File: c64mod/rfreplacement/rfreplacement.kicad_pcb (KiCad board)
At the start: 2 copper layers, 63.5 x 64.8 mm, 94 parts, among them SW1 SW_SP3T, U2 10M02SCE144, Y1 Conn_Coaxial

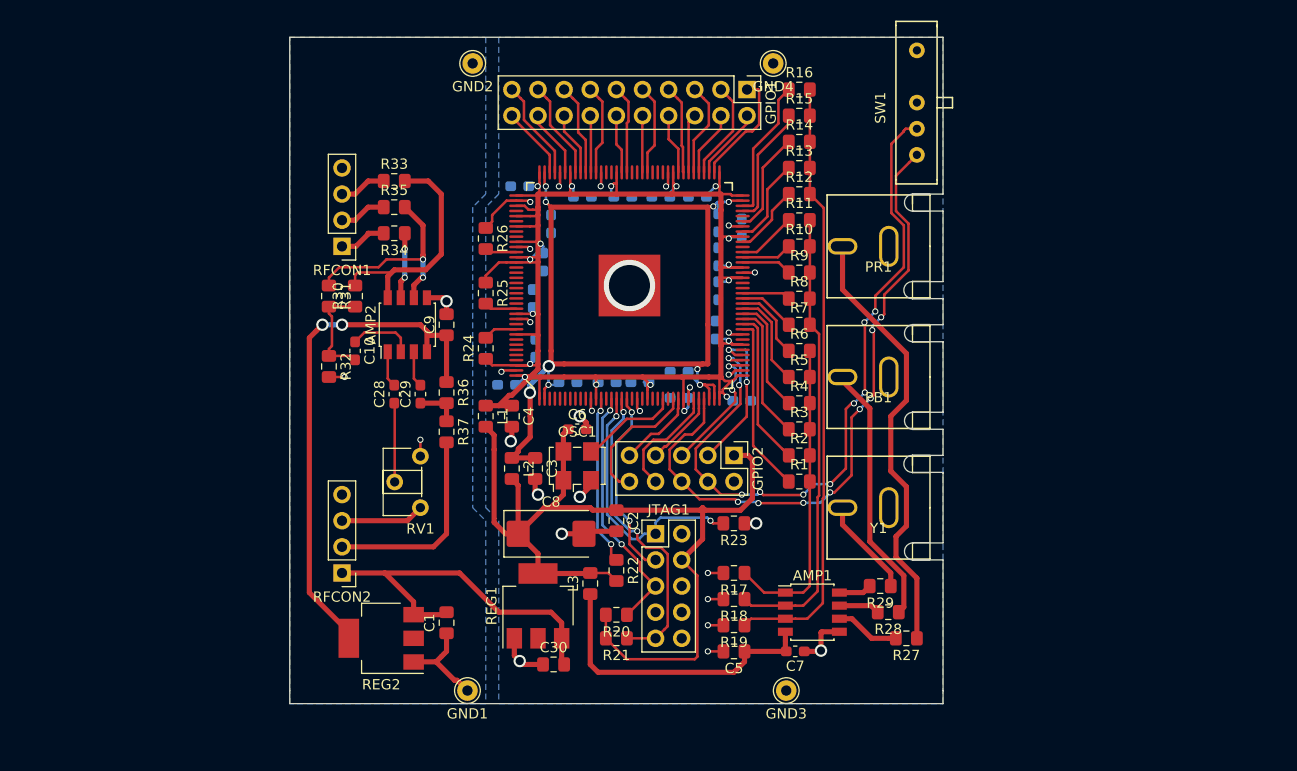
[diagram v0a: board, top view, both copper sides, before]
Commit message: C64 mod: fit rf replacement to long and short main boards
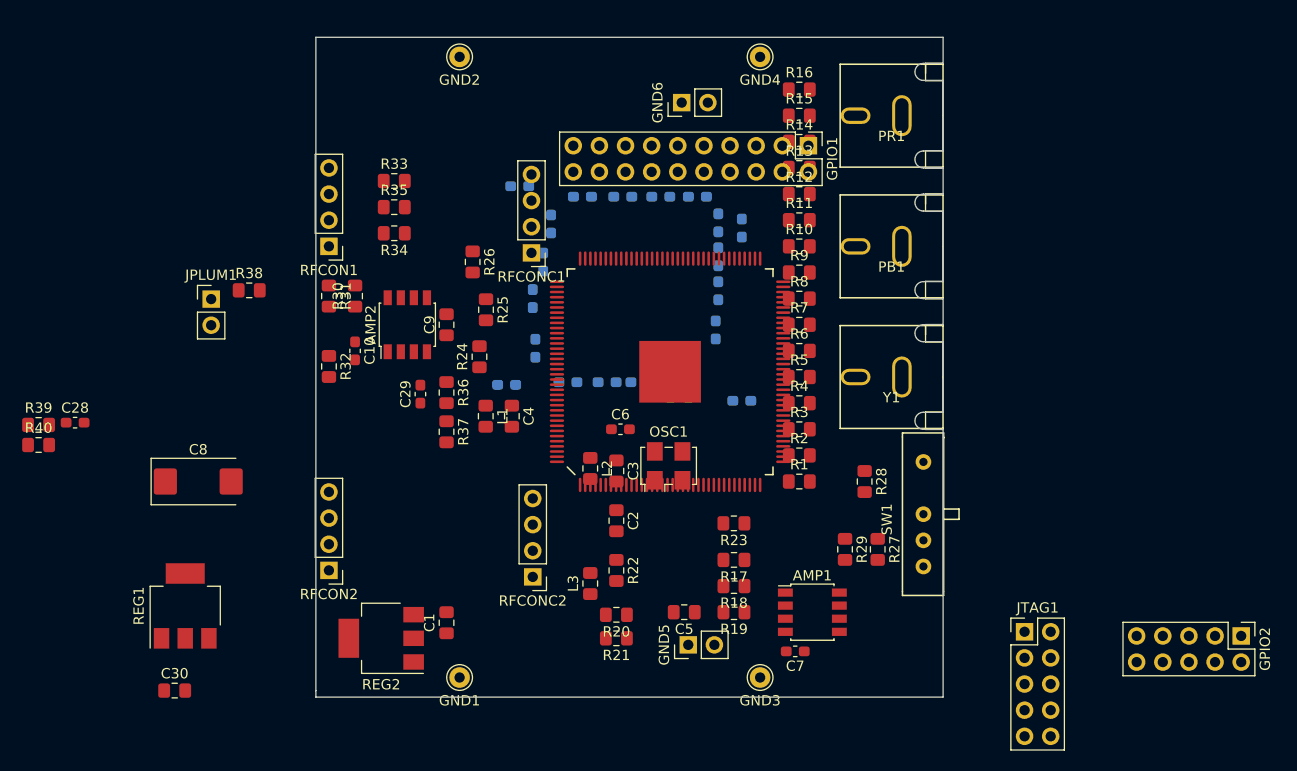
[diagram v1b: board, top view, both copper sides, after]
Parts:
- removed RV1: 1k, Potentiometer_THT:Potentiometer_ACP_CA6-H2,5_Horizontal
- added GND5: Conn_01x02, Connector_PinHeader_2.54mm:PinHeader_1x02_P2.54mm_Vertical, F.Cu at (140.3, 109.9)
- added GND6: Conn_01x02, Connector_PinHeader_2.54mm:PinHeader_1x02_P2.54mm_Vertical, F.Cu at (139.7, 57.1)
- added JPLUM1: Jumper_2_Open, Connector_PinHeader_2.54mm:PinHeader_1x02_P2.54mm_Vertical, F.Cu at (94.0, 76.2)
- added R38: 680, Resistor_SMD:R_0805_2012Metric_Pad1.15x1.40mm_HandSolder, F.Cu at (97.7, 75.4)
- added R39: 680, Resistor_SMD:R_0805_2012Metric_Pad1.15x1.40mm_HandSolder, F.Cu at (77.2, 88.5)
- added R40: 330, Resistor_SMD:R_0805_2012Metric_Pad1.15x1.40mm_HandSolder, F.Cu at (77.2, 90.4)
- added RFCONC1: Conn_01x04, Connector_PinHeader_2.54mm:PinHeader_1x04_P2.54mm_Vertical, F.Cu at (125.1, 71.8)
- added RFCONC2: Conn_01x04, Connector_PinHeader_2.54mm:PinHeader_1x04_P2.54mm_Vertical, F.Cu at (125.2, 103.3)
- R36: value 150 -> 680
- R37: value 310 -> 330
- moved GPIO2 52.3 mm to (194.1, 109.0)
- moved SW1 40.0 mm to (160.7, 97.2)
- moved JTAG1 37.1 mm to (173.0, 108.6)
- moved C30 36.9 mm to (90.4, 114.3)
- moved C8 34.7 mm to (92.7, 94.0)
- moved REG1 34.3 mm to (91.4, 106.1)
- moved C28 31.1 mm to (80.7, 88.3), turned to 0 degrees
- moved R28 12.9 mm to (157.5, 94.0), turned to 270 degrees
- moved PR1 12.8 mm to (165.1, 58.4)
- moved Y1 12.8 mm to (165.1, 83.8)
- moved PB1 12.8 mm to (165.1, 71.1)
- moved U2 9.27 mm to (138.6, 83.3)
- moved R27 9.08 mm to (158.8, 100.6), turned to 270 degrees
- moved OSC1 8.89 mm to (138.4, 92.5)
- moved GPIO1 8.09 mm to (152.0, 61.3)
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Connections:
- R36 pad 2: Net-(C29-Pad1) -> Net-(JPLUM1-Pad1)
- R37 pad 1: Net-(C29-Pad1) -> /3V3X
- R37 pad 2: /LUMA_IN -> Net-(C29-Pad1)
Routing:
- net /3V3B: track 178.1 -> 0.00 mm, vias 18 -> 0
- net /3V3A: track 98.0 -> 0.00 mm
- net /3V3C: track 97.2 -> 0.00 mm, vias 9 -> 0
- net Net-(GPIO2-Pad4): track 69.5 -> 0.00 mm, vias 10 -> 0
- net Net-(GPIO2-Pad6): track 63.8 -> 0.00 mm, vias 8 -> 0
- net Net-(AMP1-Pad3): track 59.0 -> 0.00 mm
- net GND: track 53.0 -> 0.00 mm, vias 27 -> 0
- net /3V3X: track 51.0 -> 0.00 mm, vias 2 -> 0
- net Net-(AMP1-Pad2): track 44.4 -> 0.00 mm
- net /PR: track 43.2 -> 0.00 mm
- net +12V: track 36.0 -> 0.00 mm
- net Net-(JTAG1-Pad9): track 30.6 -> 0.00 mm, vias 2 -> 0
- net Net-(AMP1-Pad1): track 30.3 -> 0.00 mm
- net /3V3D: track 29.6 -> 0.00 mm
- net Net-(JTAG1-Pad1): track 25.7 -> 0.00 mm, vias 2 -> 0
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- removed copper zone on B.Cu, net GND
- removed copper zone on B.Cu, net GNDA
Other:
- board size 63.5 x 64.8 mm -> 61 x 64.1 mm

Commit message: Layout RF replacement board
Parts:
- removed GND6: Conn_01x02, Connector_PinHeader_2.54mm:PinHeader_1x02_P2.54mm_Vertical
- removed GPIO2: Conn_02x05_Odd_Even, Connector_PinHeader_2.54mm:PinHeader_2x05_P2.54mm_Vertical
- removed PB1, PR1, Y1: Conn_Coaxial, footprints:RCA_JACK
- added J1: AudioJack4_Ground, footprints:Conrad 4pin audio jack, F.Cu at (167.0, 69.8)
- C6, C7, C9: moved to B.Cu
- C8: footprint Capacitor_Tantalum_SMD:CP_EIA-7343-15_Kemet-W_Pad2.25x2.55mm_HandSolder -> Capacitor_SMD:CP_Elec_6.3x5.8
- moved REG1 39.5 mm to (130.8, 109.2), turned to 0 degrees
- moved C8 38.6 mm to (130.8, 100.3), turned to 90 degrees
- moved C28 35.7 mm to (113.0, 73.0), turned to 90 degrees
- moved JTAG1 35.5 mm to (137.5, 109.2), turned to 90 degrees
- moved R19 35.5 mm to (162.1, 75.7), turned to 0 degrees
- moved R40 35.0 mm to (110.5, 79.8), turned to 90 degrees
- moved C30 34.4 mm to (124.5, 109.5), turned to 270 degrees
- moved GND5 33.8 mm to (162.6, 84.5), turned to 180 degrees
- moved R39 33.6 mm to (110.5, 83.8), turned to 90 degrees
- moved L1 31.5 mm to (149.1, 101.1)
- moved R18 31.3 mm to (162.1, 78.0), turned to 0 degrees
- moved JPLUM1 27.4 mm to (118.5, 88.5)
- moved C4 25.9 mm to (147.3, 97.0), turned to 180 degrees
- moved C34 24.9 mm to (143.9, 93.7), turned to 180 degrees
- moved C2 23.7 mm to (152.9, 111.1), turned to 0 degrees
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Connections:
- AMP1 pad 6: /PR1 -> /PY1
- AMP1 pad 8: /PY1 -> /PR1
- R1 pad 2: Net-(AMP1-Pad1) -> Net-(AMP1-Pad3)
- R12 pad 2: Net-(AMP1-Pad3) -> Net-(AMP1-Pad1)
- R13 pad 2: Net-(AMP1-Pad3) -> Net-(AMP1-Pad1)
- R14 pad 2: Net-(AMP1-Pad3) -> Net-(AMP1-Pad1)
- R15 pad 2: Net-(AMP1-Pad3) -> Net-(AMP1-Pad1)
- R16 pad 2: Net-(AMP1-Pad3) -> Net-(AMP1-Pad1)
- R17 pad 1: Net-(AMP1-Pad1) -> Net-(AMP1-Pad3)
- R19 pad 1: Net-(AMP1-Pad3) -> Net-(AMP1-Pad1)
- R2 pad 2: Net-(AMP1-Pad1) -> Net-(AMP1-Pad3)
- R3 pad 2: Net-(AMP1-Pad1) -> Net-(AMP1-Pad3)
- R4 pad 2: Net-(AMP1-Pad1) -> Net-(AMP1-Pad3)
- R5 pad 2: Net-(AMP1-Pad1) -> Net-(AMP1-Pad3)
- R6 pad 2: Net-(AMP1-Pad1) -> Net-(AMP1-Pad3)
- SW1 pad 1: Net-(GPIO2-Pad6) -> Net-(SW1-Pad1)
- U2 pad 33: Net-(GPIO2-Pad6) -> Net-(U2-Pad33)
- U2 pad 39: Net-(GPIO2-Pad5) -> Net-(SW1-Pad1)
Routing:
- net /3V3B: track 0.00 -> 178.8 mm, vias 0 -> 17
- net /3V3C: track 0.00 -> 92.2 mm, vias 0 -> 9
- net /3V3A: track 0.00 -> 74.1 mm, vias 0 -> 2
- net /3V3X: track 0.00 -> 59.7 mm, vias 0 -> 3
- net /PB: track 0.00 -> 49.7 mm, vias 0 -> 1
- net GND: track 0.00 -> 48.6 mm, vias 0 -> 25
- net /PR: track 0.00 -> 48.1 mm, vias 0 -> 1
- net Net-(AMP1-Pad1): track 0.00 -> 45.9 mm
- net /Y: track 0.00 -> 44.0 mm, vias 0 -> 1
- net /COMPOSITE_OUT: track 0.00 -> 43.9 mm, vias 0 -> 3
- net +12V: track 0.00 -> 39.9 mm
- net Net-(AMP1-Pad2): track 0.00 -> 36.0 mm
- net /CHROMA_IN: track 0.00 -> 34.6 mm, vias 0 -> 2
- net /LUMA_OUT: track 0.00 -> 34.3 mm, vias 0 -> 2
- net /CHROMA_OUT: track 0.00 -> 34.2 mm
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- added copper zone on B.Cu, net GND
- added copper zone on B.Cu, net GNDA
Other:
- outline, holes or cut-outs redrawn

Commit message: Finished RF replacement  board for C64
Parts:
- C9: moved to F.Cu
- JPLUM1: footprint Connector_PinHeader_2.54mm:PinHeader_1x02_P2.54mm_Vertical -> Jumper:SolderJumper-2_P1.3mm_Open_RoundedPad1.0x1.5mm
- moved C9 12.4 mm to (120.1, 78.2), turned to 270 degrees
- moved JPLUM1 3.68 mm to (118.5, 92.2), turned to 270 degrees
- moved C20 2.47 mm to (130.3, 93.5), turned to 0 degrees
- moved C21 2.05 mm to (129.7, 71.5), turned to 0 degrees
- moved RFCONC1 0.64 mm to (125.7, 71.1)
- moved RFCONC2 0.64 mm to (125.7, 102.6)
- moved SW1 0.64 mm to (160.7, 96.5)
- moved R19 0.51 mm to (162.1, 75.2)
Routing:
- net Net-(SW1-Pad2): track 21.9 -> 32.7 mm
- net +12V: track 39.9 -> 44.4 mm
- net /3V3B: track 178.8 -> 182.0 mm
- net Net-(JPLUM1-Pad1): track 3.09 -> 6.12 mm
- net GNDA: track 11.1 -> 12.6 mm, vias 4 -> 5
- net /3V3C: track 92.2 -> 93.5 mm
- net Net-(AMP2-Pad8): track 16.8 -> 15.5 mm
- net Net-(AMP1-Pad2): track 36.0 -> 35.0 mm
- net Net-(AMP1-Pad1): track 45.9 -> 45.1 mm, vias 0 -> 2
- net Net-(SW1-Pad1): track 24.3 -> 25.1 mm
- net /LUMA_OUT: track 34.3 -> 34.9 mm
- net /COMPOSITE_OUT: track 43.9 -> 44.5 mm
- net /CHROMA_OUT: track 34.2 -> 34.9 mm
- net /CHROMA_IN: track 34.6 -> 35.2 mm
- net /LUMA_IN: track 33.7 -> 34.3 mm
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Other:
- board text added: "C64 Video Enhancement github.com/c0pperdragon"
- board text added: "Close: 9V VIC Open: 5V VIC"
- board text added: "U2"
